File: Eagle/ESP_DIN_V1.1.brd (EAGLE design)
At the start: 64.9 x 83.9 mm, 60 parts, among them IC1 TLP185, K1 HF46F/005-HS1, K2 44.62.9.006.0000, T1 BC817, T2 BC817, U1 ESP8266-12, U2 RXB6, U3 LM1117-3.3, X1 KF350-3.5-2P, X2 KF350-3.50-3P, X3 SMA-EDGE-UFLLONG, X4 KF301-5.08-2P, X5 KF301-5.08-2P, X6 KF301-5.08-3P, X8 KF301-5.08-2P

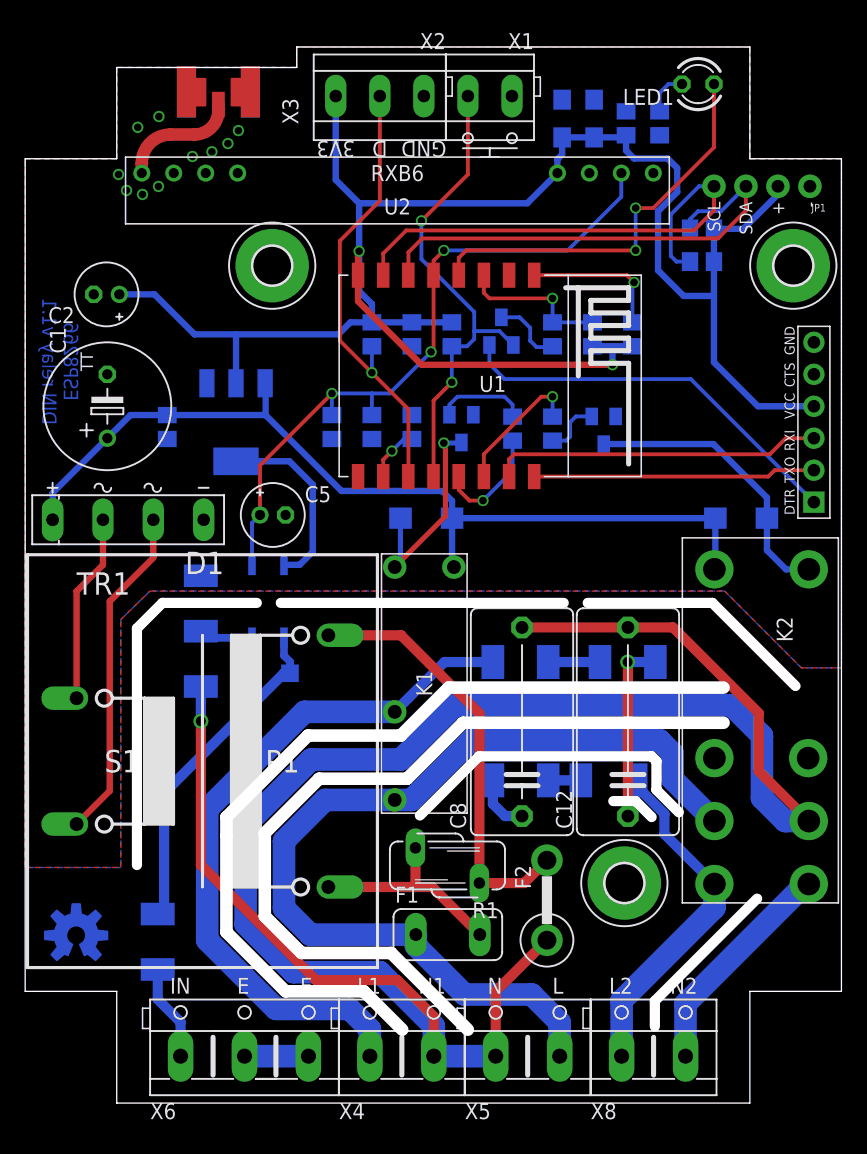
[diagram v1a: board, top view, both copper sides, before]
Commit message: milling corrections
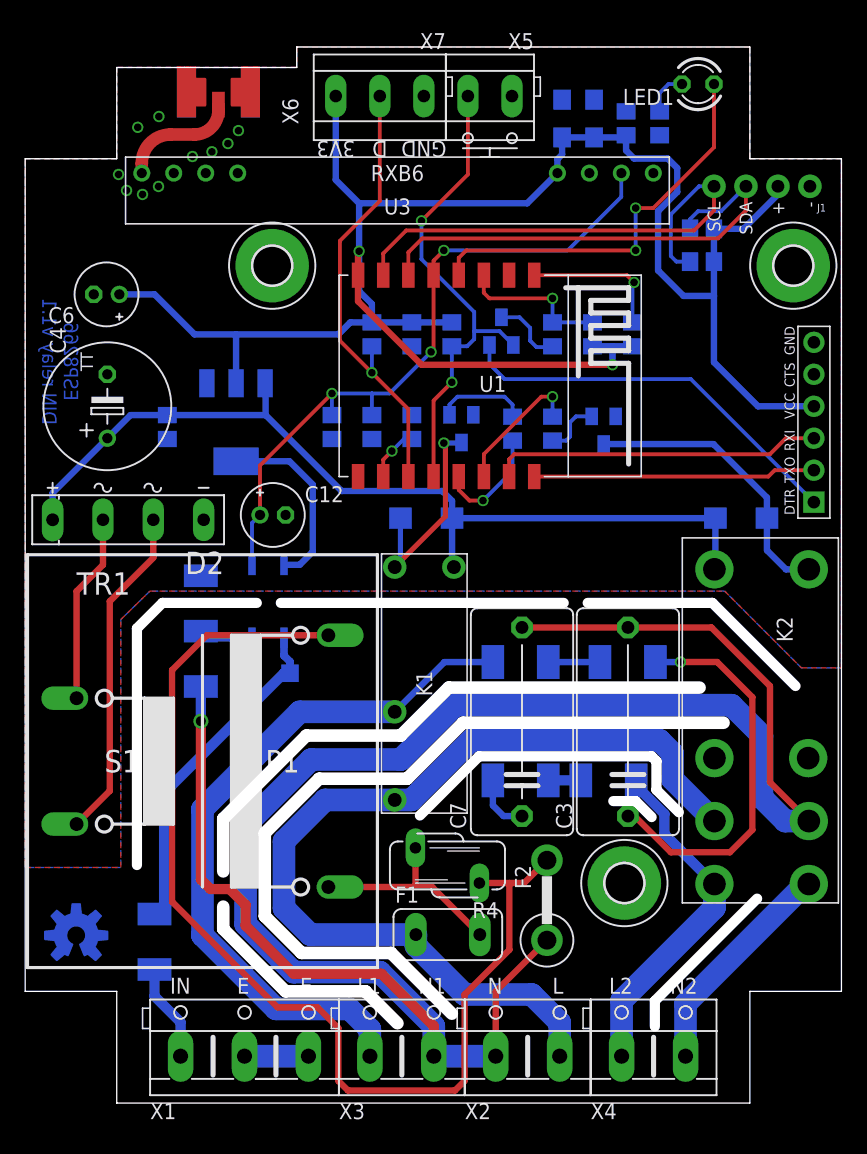
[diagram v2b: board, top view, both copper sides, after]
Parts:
- removed JP3: FTDI_CONN, my-connectors:FTDI
- removed X8: KF301-5.08-2P, my-connectors:KF301-5.08-2P
- added J1: (no value), SparkFun-Connectors:1X04_NO_SILK
- added X7: KF350-3.50-3P, my-connectors:KF350-3.50-3P
- C1: value 1000uF/16V -> 100n; device rcl:TT5D10 -> rcl:C0805
- C12: value R463I24705001K -> 100uF/16V; device rcl:C150-084X183 -> rcl:E2-5
- C2, C5: value 100uF/16V -> 100n; device rcl:E2-5 -> rcl:C0805
- C3, C7: value 100n -> R463I24705001K; device rcl:C0805 -> rcl:C150-084X183
- C4: value 100n -> 1000uF/16V; device rcl:C0805 -> rcl:TT5D10
- C6: value 100n -> 100uF/16V; device rcl:C0805 -> rcl:E2-5
- C8: value R463I24705001K -> 100n; device rcl:C150-084X183 -> rcl:C0805
- D1: value (none) -> S1B; device my-diode:KBP307 -> my-diode:DO214AC
- D2: value S1B -> (none); device my-diode:DO214AC -> my-diode:KBP307
- D3: value SL1M -> S1B; device my-diode:SOD123 -> my-diode:DO214AC
- D5: value S1B -> SL1M; device my-diode:DO214AC -> my-diode:SOD123
- JP1: value (none) -> FTDI_CONN; device SparkFun-Connectors:1X04_NO_SILK -> my-connectors:FTDI
- R1: value S07K275 -> 820R; device varistor:S07K250 -> rcl:R0805
- R10: value 820R -> 10K
- R11: value 200K -> 160R
- R12: value 4K7 -> 160R; device rcl:R0805 -> rcl:R2010
- R13: value 10K -> 200K; device rcl:R0805 -> rcl:R2010
- R14, R15: value 160R -> 4K7; device rcl:R2010 -> rcl:R0805
- R16: value 160R -> 10K; device rcl:R2010 -> rcl:R0805
- R2: value 10K -> 1K
- R4: value 10K -> S07K275; device rcl:R0805 -> varistor:S07K250
- R7: value 1K -> 160R; device rcl:R0805 -> rcl:R2010
- R8: value 4K7 -> 1K
- R9: value 1K -> 10K
- U2: value RXB6 -> LM1117-3.3; device my-modules:RXB6 -> my-power:SOT223
- U3: value LM1117-3.3 -> RXB6; device my-power:SOT223 -> my-modules:RXB6
- X1: value KF350-3.5-2P -> KF301-5.08-3P; device my-connectors:KF350-3.50-2P -> my-connectors:KF301-5.08-3P
- X2: value KF350-3.50-3P -> KF301-5.08-2P; device my-connectors:KF350-3.50-3P -> my-connectors:KF301-5.08-2P
- X3: value SMA-EDGE-UFLLONG -> KF301-5.08-2P; device my-connectors:SMA_EDGE_UFL_W -> my-connectors:KF301-5.08-2P
- X5: value KF301-5.08-2P -> KF350-3.5-2P; device my-connectors:KF301-5.08-2P -> my-connectors:KF350-3.50-2P
- X6: value KF301-5.08-3P -> SMA-EDGE-UFLLONG; device my-connectors:KF301-5.08-3P -> my-connectors:SMA_EDGE_UFL_W
- moved X3 80.0 mm to (32.4, 6.15), turned to 0 degrees
- moved X1 78.7 mm to (19.9, 6.15), turned to 0 degrees
- moved X6 78.7 mm to (17.8, 84.8), turned to 270 degrees
- moved X2 77.2 mm to (42.4, 6.15), turned to 0 degrees
- moved X5 76.3 mm to (39.4, 82.4), turned to 180 degrees
- moved R1 61.3 mm to (52.8, 80.3), flipped to the bottom
- moved C7 48.3 mm to (41.9, 32.7), flipped to the top
- moved C8 48.3 mm to (50.2, 80.3), flipped to the bottom
- moved R13 44.4 mm to (12.7, 15.2)
- moved R4 43.7 mm to (36.0, 21.3), flipped to the top, turned to 90 degrees
- moved R12 43.7 mm to (41.8, 28.1)
- moved C3 43.4 mm to (50.3, 32.7), flipped to the top, turned to 90 degrees
- moved D3 39.6 mm to (59.3, 48.9), turned to 180 degrees
- moved D5 39.6 mm to (21.7, 36.6), turned to 0 degrees
- moved R11 38.0 mm to (48.8, 28.1), turned to 180 degrees
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- renumbered D7 to D4, T1 to Q1, T2 to Q2
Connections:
- net +3V3: now also C2.1, C6.+, C8.1, J1.2, JP1.P$4, R14.2, R15.1, R9.2, U2.2, U2.4, U3.VCC, U3.VCC@1, X7.3; no longer C2.+, C4.1, C7.1, JP1.2, JP3.P$4, R12.2, R4.2, R8.1, U2.VCC, U2.VCC@1, U3.2, U3.4, X2.3
- net 1-WIRE: now also R15.2, X7.2; no longer R8.2, X2.2
- net ANT: now also U3.ANT, X6.P; no longer U2.ANT, X3.P
- net BUTTON: now also R9.1, X5.2; no longer R5.1, X1.2
- net CH: now also C1.1; no longer C6.1
- net DTR: now also JP1.P$1; no longer JP3.P$1
- net E: now also X1.2, X1.3; no longer X6.2, X6.3
- net GND: now also C12.-, C2.2, C4.-, C5.2, C6.-, C8.2, D2.-, J1.1, JP1.P$6, R1.1, R16.1, U2.1, U3.GND, U3.GND@1, U3.GND@2, X5.1, X6.GND@1, X6.GND@2, X6.GND@3, X6.GND@4, X7.1; no longer C1.-, C2.-, C3.2, C4.2, C5.-, C7.2, D1.-, JP1.1, JP3.P$6, R13.1, R2.1, U2.GND, U2.GND@1, U2.GND@2, U3.1, X1.1, X2.1, X3.GND@1, X3.GND@2, X3.GND@3, X3.GND@4
- net GPIO15: now also R10.2; no longer R2.2
- net IN: now also R13.1, X1.1; no longer R11.1, X6.1
- net K1_POLE1: now also D1.A; no longer D2.A
- net K2_POLE1: now also D3.A; no longer D5.A
- net L: now also X2.2; no longer X5.2
- net L1_OUT: now also X3.1; no longer X4.1
- net L2_OUT: now also R11.2, X4.1; no longer R16.2, X8.1
- net N: now also C3.2, C7.2, X2.1, X3.2; no longer C12.2, C8.2, X4.2, X5.1
- net N$10: now also R5.1; no longer R3.1
- net N$11: now also C1.2, R3.1; no longer C6.2, R4.1
- net N$12: now also R7.2; no longer R14.2
- net N$13: now also C7.1, R12.1; no longer C8.1, R15.1
- net N$14: now also R4.1; no longer R1.1
- net N$15: now also R11.1, R12.2; no longer R15.2, R16.1
- net N$16: now also R2.1; no longer R7.1
- net N$2: now also R8.1; no longer R9.1
- net N$3: now also D2.AC1; no longer D1.AC1
- net N$4: now also D2.AC2; no longer D1.AC2
- net N$5: now also R1.2; no longer R10.2
- net N$6: now also D5.A; no longer D3.A
- net N$7: now also D5.C, R13.2; no longer D3.C, R11.2
- net N$8: now also R4.2; no longer R1.2
- net N$9: now also C3.1, R7.1; no longer C12.1, R14.1
- net N2_OUT: now also X4.2; no longer X8.2
- net RELAY1: now also R2.2; no longer R7.2
- net RELAY2: now also R8.2; no longer R9.2
- net RF: now also C12.+, R16.2, U3.DATA; no longer C5.+, R13.2, U2.DATA
- net RX: now also JP1.P$3; no longer JP3.P$3
- net SCL: now also J1.4, R14.1; no longer JP1.4, R12.1
- net SDA: now also J1.3; no longer JP1.3
- net TX: now also JP1.P$2; no longer JP3.P$2
- net VCC: now also C4.+, C5.1, D1.C, D2.+, D3.C, U2.3; no longer C1.+, C3.1, D1.+, D2.C, D5.C, U3.3
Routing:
- net N$14: track 34.2 -> 87.5 mm
- net N$9: track 14.4 -> 31.2 mm
- net N: track 172.5 -> 175.5 mm
- net L1_OUT: track 55.9 -> 56.5 mm
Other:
- outline, holes or cut-outs redrawn

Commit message: IN & RF together
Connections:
- removed net GPIO15: R10.2, U1.GPIO15
- removed net N$1: LED1.A, U1.GPIO16
- new net INPUT: R13.1, X1.1
- new net LED: LED1.A, R10.2, U1.GPIO15
- net IN: now also C11.1, C12.+, IC1.3, R16.2, U1.GPIO16; no longer R13.1, X1.1
- net RF: no longer C11.1, C12.+, IC1.3, R16.2
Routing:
- net LED: track 0.00 -> 55.8 mm, vias 0 -> 4
- net RF: track 55.2 -> 20.1 mm, vias 3 -> 1
- net N$1: track 32.3 -> 0.00 mm, vias 2 -> 0
- net IN: track 7.75 -> 34.0 mm, vias 0 -> 2
- net INPUT: track 0.00 -> 7.75 mm
- net GPIO15: track 4.30 -> 0.00 mm, vias 1 -> 0
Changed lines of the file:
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@@
 <?xml version="1.0" encoding="utf-8"?>
 <!DOCTYPE eagle SYSTEM "eagle.dtd">
-<eagle version="9.0.0">
+<eagle version="9.0.1">
 <drawing>
 <settings>
@@
 <text x="34.1" y="78.865" size="1.27" layer="21" font="vector" ratio="15" rot="SR180" align="bottom-center">GND</text>
 <text x="27.1" y="78.865" size="1.27" layer="21" font="vector" ratio="15" rot="SR180" align="bottom-center">3V3</text>
-<circle x="37.6" y="79.0825" radius="0.4" width="0.1524" layer="21"/>
-<circle x="41.1" y="79.0825" radius="0.4" width="0.1524" layer="21"/>
-<wire x1="37.2" y1="78.2825" x2="39.332" y2="78.2825" width="0.1524" layer="21"/>
-<wire x1="39.332" y1="78.2825" x2="41.5" y2="78.2825" width="0.1524" layer="21"/>
-<wire x1="38.6" y1="77.5825" x2="39.332" y2="77.5825" width="0.1524" layer="21"/>
-<wire x1="39.332" y1="77.5825" x2="40.1" y2="77.5825" width="0.1524" layer="21"/>
-<wire x1="39.332" y1="77.5825" x2="39.332" y2="78.2825" width="0.1524" layer="21"/>
+<wire x1="37.2" y1="78.5365" x2="39.332" y2="78.5365" width="0.1524" layer="21"/>
+<wire x1="39.332" y1="78.5365" x2="41.5" y2="78.5365" width="0.1524" layer="21"/>
+<wire x1="38.6" y1="77.8365" x2="39.332" y2="77.8365" width="0.1524" layer="21"/>
+<wire x1="39.332" y1="77.8365" x2="40.1" y2="77.8365" width="0.1524" layer="21"/>
+<wire x1="39.332" y1="77.8365" x2="39.332" y2="78.5365" width="0.1524" layer="21"/>
 <wire x1="19.803" y1="6.15" x2="24.803" y2="6.15" width="1.8" layer="30"/>
 <wire x1="26.51" y1="39.591" x2="26.51" y2="26.83" width="1.8" layer="29"/>
@@
 <wire x1="37.531" y1="62.55" x2="38.1" y2="63.119" width="0.3048" layer="16"/>
 <wire x1="38.1" y1="63.119" x2="38.1" y2="63.754" width="0.3048" layer="16"/>
-<via x="36.322" y="59.69" extent="1-16" drill="0.6"/>
-<wire x1="36.322" y1="59.69" x2="36.322" y2="62.55" width="0.3048" layer="16"/>
+<via x="36.322" y="60.071" extent="1-16" drill="0.6"/>
+<wire x1="36.322" y1="60.071" x2="36.322" y2="62.55" width="0.3048" layer="16"/>
 <wire x1="33.909" y1="69.469" x2="33.909" y2="72.517" width="0.3048" layer="16"/>
 <wire x1="38.1" y1="63.754" x2="38.1" y2="65.278" width="0.3048" layer="16"/>
-<wire x1="38.1" y1="65.278" x2="34.925" y2="68.453" width="0.3048" layer="16"/>
-<wire x1="34.925" y1="68.453" x2="33.909" y2="69.469" width="0.3048" layer="16"/>
-<wire x1="34.87" y1="58.238" x2="36.322" y2="59.69" width="0.3048" layer="1"/>
-<wire x1="34.87" y1="52.198" x2="34.87" y2="58.238" width="0.3048" layer="1"/>
+<wire x1="38.1" y1="65.278" x2="33.909" y2="69.469" width="0.3048" layer="16"/>
+<wire x1="34.87" y1="58.619" x2="36.322" y2="60.071" width="0.3048" layer="1"/>
+<wire x1="34.87" y1="52.198" x2="34.87" y2="58.619" width="0.3048" layer="1"/>
 <wire x1="37.6" y1="82.43" x2="37.6" y2="76.208" width="0.3048" layer="1"/>
 <wire x1="37.6" y1="76.208" x2="33.909" y2="72.517" width="0.3048" layer="1"/>
@@
 <wire x1="34.87" y1="68.198" x2="34.87" y2="69.3505" width="0.3048" layer="1"/>
 <wire x1="34.87" y1="69.3505" x2="35.687" y2="70.1675" width="0.3048" layer="1"/>
-<contactref element="IC1" pad="3"/>
-<contactref element="R16" pad="2"/>
-<contactref element="C11" pad="1"/>
-<contactref element="C12" pad="+"/>
-<wire x1="20.447" y1="45.191" x2="20.447" y2="48.514" width="0.3048" layer="16"/>
-<wire x1="20.447" y1="48.514" x2="21.082" y2="49.149" width="0.3048" layer="16"/>
-<via x="26.797" y="58.801" extent="1-16" drill="0.6"/>
-<wire x1="34.87" y1="68.198" x2="34.87" y2="62.302" width="0.3048" layer="1"/>
-<wire x1="34.87" y1="62.302" x2="34.671" y2="62.103" width="0.3048" layer="1"/>
-<via x="34.671" y="62.103" extent="1-16" drill="0.6"/>
-<wire x1="21.082" y1="49.149" x2="21.082" y2="53.086" width="0.3048" layer="1"/>
-<wire x1="21.082" y1="53.086" x2="26.797" y2="58.801" width="0.3048" layer="1"/>
-<wire x1="26.797" y1="58.801" x2="29.972" y2="58.801" width="0.3048" layer="16"/>
-<wire x1="29.972" y1="58.801" x2="31.369" y2="58.801" width="0.3048" layer="16"/>
-<wire x1="31.369" y1="58.801" x2="34.671" y2="62.103" width="0.3048" layer="16"/>
-<wire x1="29.972" y1="57.084" x2="29.972" y2="58.801" width="0.3048" layer="16"/>
-<wire x1="26.797" y1="57.084" x2="26.797" y2="58.801" width="0.3048" layer="16"/>
 </signal>
 <signal name="ANT">
@@
 <wire x1="64.4065" y1="19.8295" x2="64.683" y2="19.8295" width="1.8" layer="16"/>
 </signal>
-<signal name="N$1">
-<contactref element="U1" pad="GPIO16"/>
-<contactref element="LED1" pad="A"/>
-<wire x1="36.87" y1="69.5725" x2="36.87" y2="68.198" width="0.3048" layer="1"/>
-<via x="50.927" y="70.1675" extent="1-16" drill="0.6"/>
-<wire x1="36.87" y1="69.5725" x2="37.465" y2="70.1675" width="0.3048" layer="1"/>
-<via x="50.927" y="73.533" extent="1-16" drill="0.6"/>
-<wire x1="50.927" y1="73.533" x2="50.927" y2="70.1675" width="0.3048" layer="16"/>
-<wire x1="37.465" y1="70.1675" x2="50.927" y2="70.1675" width="0.3048" layer="1"/>
-<wire x1="50.927" y1="73.533" x2="52.324" y2="73.533" width="0.3048" layer="1"/>
-<wire x1="57.15" y1="78.359" x2="57.15" y2="83.3825" width="0.3048" layer="1"/>
-<wire x1="52.324" y1="73.533" x2="57.15" y2="78.359" width="0.3048" layer="1"/>
-</signal>
 <signal name="N$5">
-<contactref element="LED1" pad="K"/>
 <contactref element="R1" pad="2"/>
 <wire x1="52.832" y1="81.214" x2="52.832" y2="82.677" width="0.3048" layer="16"/>
+<wire x1="52.832" y1="82.677" x2="53.5375" y2="83.3825" width="0.3048" layer="16"/>
+<contactref element="LED1" pad="K"/>
 <wire x1="53.5375" y1="83.3825" x2="54.61" y2="83.3825" width="0.3048" layer="16"/>
-<wire x1="52.832" y1="82.677" x2="53.5375" y2="83.3825" width="0.3048" layer="16"/>
-</signal>
-<signal name="GPIO15">
+</signal>
+<signal name="LED">
 <contactref element="U1" pad="GPIO15"/>
 <contactref element="R10" pad="2"/>
@@
 <wire x1="33.147" y1="55.184" x2="32.5145" y2="55.184" width="0.3048" layer="16"/>
 <wire x1="32.5145" y1="55.184" x2="31.5595" y2="54.229" width="0.3048" layer="16"/>
+<contactref element="LED1" pad="A"/>
+<wire x1="57.15" y1="83.3825" x2="57.15" y2="79.121" width="0.3048" layer="1"/>
+<wire x1="57.15" y1="79.121" x2="51.054" y2="73.025" width="0.3048" layer="1"/>
+<via x="51.054" y="73.025" extent="1-16" drill="0.6"/>
+<wire x1="33.147" y1="55.184" x2="34.356" y2="55.184" width="0.3048" layer="16"/>
+<wire x1="34.925" y1="55.753" x2="34.925" y2="58.039" width="0.3048" layer="16"/>
+<wire x1="34.925" y1="58.039" x2="36.195" y2="59.309" width="0.3048" layer="16"/>
+<wire x1="52.07" y1="59.309" x2="52.959" y2="58.42" width="0.3048" layer="16"/>
+<via x="52.959" y="58.42" extent="1-16" drill="0.6"/>
+<wire x1="52.959" y1="58.42" x2="52.959" y2="67.818" width="0.3048" layer="1"/>
+<wire x1="52.959" y1="67.818" x2="51.054" y2="69.723" width="0.3048" layer="1"/>
+<via x="51.054" y="69.723" extent="1-16" drill="0.6"/>
+<wire x1="51.054" y1="69.723" x2="51.054" y2="73.025" width="0.3048" layer="16"/>
+<wire x1="34.356" y1="55.184" x2="34.925" y2="55.753" width="0.3048" layer="16"/>
+<wire x1="36.195" y1="59.309" x2="52.07" y2="59.309" width="0.3048" layer="16"/>
 </signal>
 <signal name="N$9">
@@
 </signal>
 <signal name="IN">
-<contactref element="R13" pad="1"/>
-<contactref element="X1" pad="1"/>
-<wire x1="12.7" y1="13.04" x2="12.7" y2="10.922" width="0.8128" layer="16"/>
-<wire x1="14.77" y1="8.852" x2="14.77" y2="6.15" width="0.8128" layer="16"/>
-<wire x1="12.7" y1="10.922" x2="14.77" y2="8.852" width="0.8128" layer="16"/>
+<contactref element="U1" pad="GPIO16"/>
+<contactref element="IC1" pad="3"/>
+<contactref element="R16" pad="2"/>
+<contactref element="C11" pad="1"/>
+<contactref element="C12" pad="+"/>
+<wire x1="20.447" y1="45.191" x2="20.447" y2="48.514" width="0.3048" layer="16"/>
+<wire x1="20.447" y1="48.514" x2="21.082" y2="49.149" width="0.3048" layer="16"/>
+<wire x1="26.797" y1="57.084" x2="28.448" y2="57.084" width="0.3048" layer="16"/>
+<wire x1="28.448" y1="57.084" x2="29.972" y2="57.084" width="0.3048" layer="16"/>
+<wire x1="36.87" y1="68.198" x2="36.87" y2="65.699" width="0.3048" layer="1"/>
+<wire x1="36.87" y1="65.699" x2="34.671" y2="63.5" width="0.3048" layer="1"/>
+<via x="34.671" y="63.5" extent="1-16" drill="0.6"/>
+<wire x1="34.671" y1="63.5" x2="34.671" y2="60.198" width="0.3048" layer="16"/>
+<wire x1="30.988" y1="59.309" x2="29.972" y2="58.293" width="0.3048" layer="16"/>
+<wire x1="29.972" y1="58.293" x2="29.972" y2="57.084" width="0.3048" layer="16"/>
+<wire x1="34.671" y1="60.198" x2="33.782" y2="59.309" width="0.3048" layer="16"/>
+<wire x1="33.782" y1="59.309" x2="30.988" y2="59.309" width="0.3048" layer="16"/>
+<wire x1="21.082" y1="49.149" x2="28.448" y2="56.515" width="0.3048" layer="1"/>
+<wire x1="28.448" y1="56.515" x2="28.448" y2="57.084" width="0.3048" layer="1"/>
+<via x="28.448" y="57.084" extent="1-16" drill="0.6"/>
 </signal>
 <signal name="E">
@@
 <wire x1="16.911" y1="39.391" x2="20.447" y2="39.391" width="0.6096" layer="16"/>
 </signal>
+<signal name="INPUT">
+<contactref element="R13" pad="1"/>
+<contactref element="X1" pad="1"/>
+<wire x1="14.77" y1="8.852" x2="14.77" y2="6.15" width="0.8128" layer="16"/>
+<wire x1="14.77" y1="8.852" x2="12.7" y2="10.922" width="0.8128" layer="16"/>
+<wire x1="12.7" y1="10.922" x2="12.7" y2="13.04" width="0.8128" layer="16"/>
+</signal>
 </signals>
